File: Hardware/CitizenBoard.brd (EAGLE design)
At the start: 50 x 50 mm, 30 parts, among them IC1 MEGA8-P, J1 DCJ0202, J2 AUDIO-JACK-3.5, Y1 16MHz

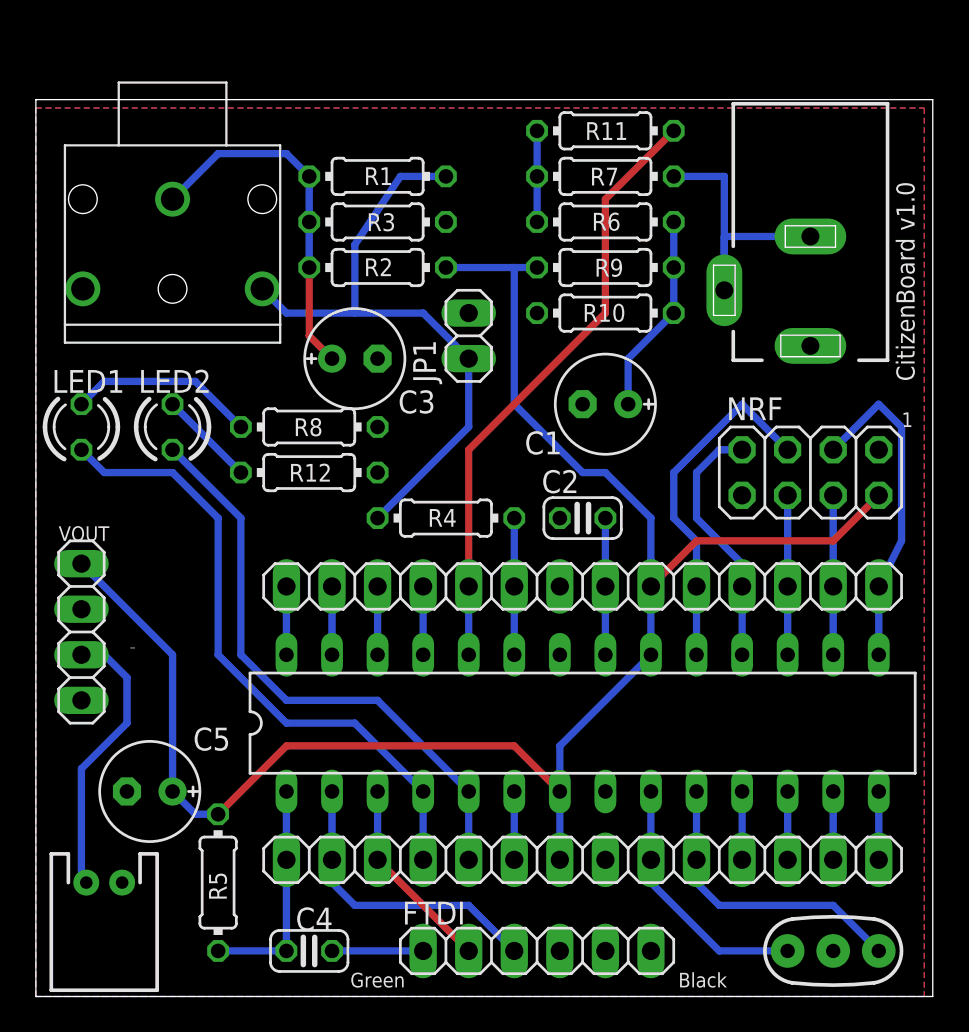
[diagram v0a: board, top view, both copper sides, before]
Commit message: Divers corrections de placement
Déplacement vers le haut de R1, R2, R3 et C3, pour les éloigner de R8.
Marquage de la polarisation des diodes et des condensateurs sur le silk.
Décalage du connecteur FTDI pour ne pas entrer en collision avec NRF
Décalage de C1 pour la même raison
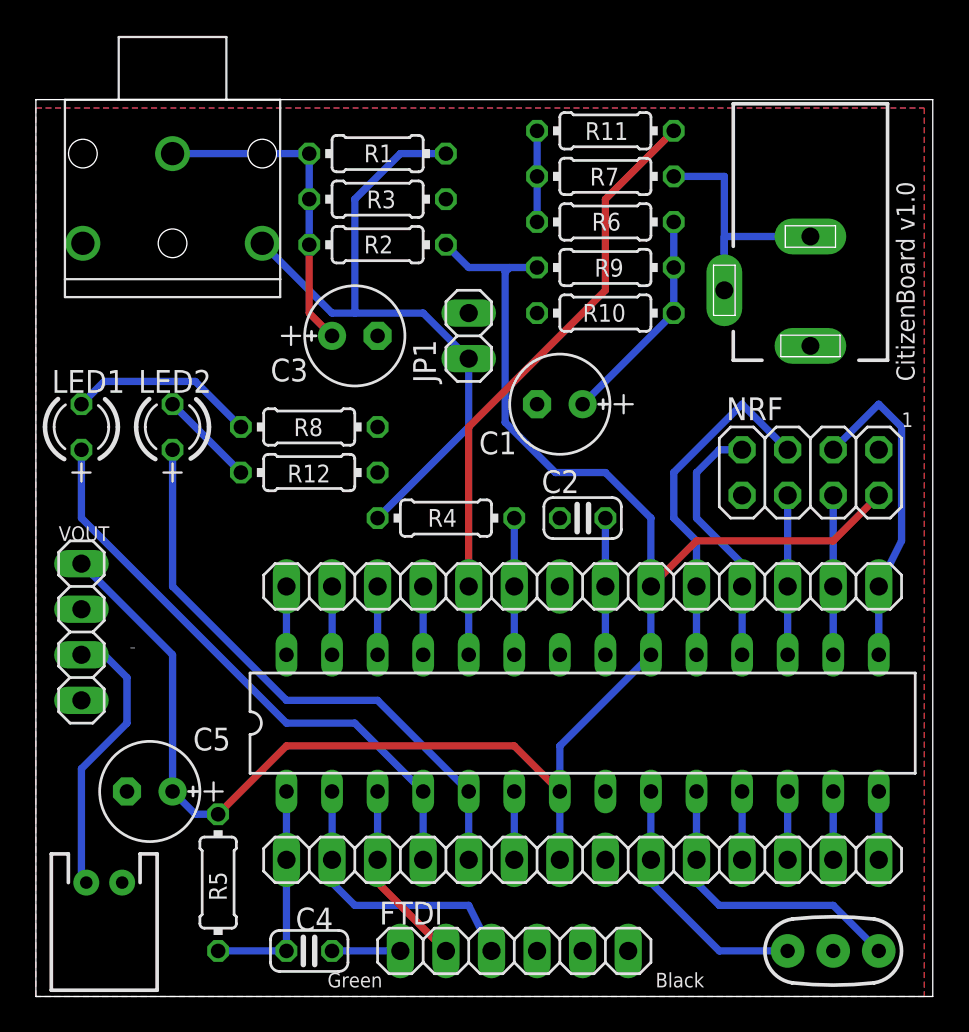
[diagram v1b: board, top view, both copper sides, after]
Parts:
- moved C1 2.54 mm to (29.2, 33.0)
- moved J2 2.54 mm to (7.62, 47.0)
- moved R1 1.27 mm to (19.1, 47.0)
- moved R3 1.27 mm to (19.1, 44.5)
- moved FTDI 1.27 mm to (26.7, 2.54)
- moved C3 1.27 mm to (17.8, 36.8)
- moved R2 1.27 mm to (19.1, 41.9)
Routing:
- net N: track 35.0 -> 37.6 mm
- net D2: track 35.2 -> 33.0 mm
- net VCC: track 98.5 -> 100.2 mm
- net N$4: track 19.9 -> 18.3 mm
- net N$3: track 5.08 -> 3.81 mm
- net N$11: track 11.2 -> 12.3 mm
- net RX: track 16.8 -> 16.1 mm
- net TX: track 11.0 -> 10.5 mm

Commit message: Correction de l'empreinte du jack
Et modification de tracés pour le champ de masse
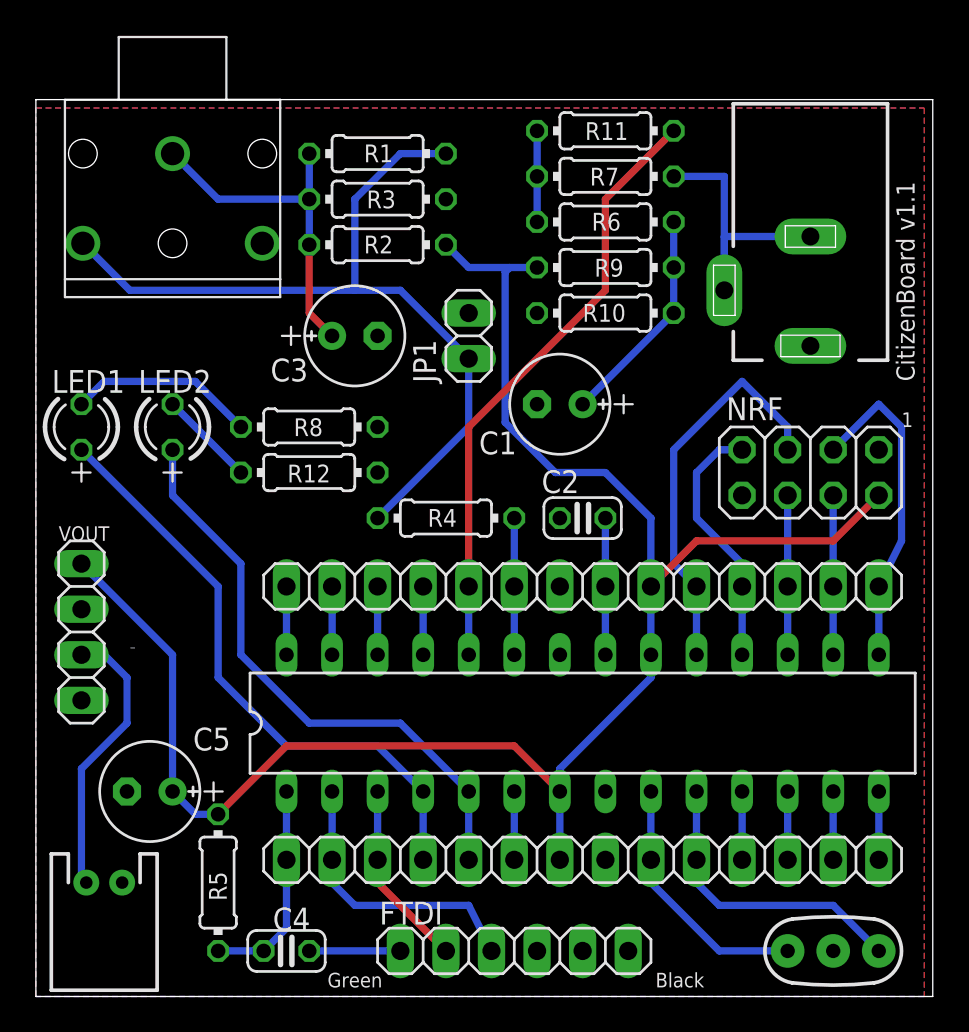
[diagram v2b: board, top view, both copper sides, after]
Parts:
- moved C4 1.27 mm to (14.0, 2.54)
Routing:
- net N: track 37.6 -> 46.4 mm
- net SCK: track 19.7 -> 22.2 mm
- net N$3: track 3.81 -> 5.08 mm
- net N$4: track 18.3 -> 19.4 mm
- net D2: track 33.0 -> 33.7 mm
- net RESET: track 12.7 -> 12.0 mm
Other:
- board text added: "CitizenBoard v1.1"
- board text removed: "CitizenBoard v1.0"
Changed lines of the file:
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@@
 <setting verticaltext="up"/>
 </settings>
-<grid distance="0.01" unitdist="inch" unit="inch" style="dots" multiple="1" display="yes" altdistance="0.025" altunitdist="inch" altunit="inch"/>
+<grid distance="0.05" unitdist="inch" unit="inch" style="dots" multiple="1" display="yes" altdistance="0.025" altunitdist="inch" altunit="inch"/>
 <layers>
-<layer number="1" name="Top" color="4" fill="1" visible="yes" active="yes"/>
+<layer number="1" name="Top" color="4" fill="1" visible="no" active="yes"/>
 <layer number="16" name="Bottom" color="1" fill="1" visible="yes" active="yes"/>
 <layer number="17" name="Pads" color="2" fill="1" visible="yes" active="yes"/>
@@
 <rectangle x1="4.84631875" y1="47.64608125" x2="5.94868125" y2="47.6885" layer="22"/>
 <text x="0" y="-0.21081875" size="0.08381875" layer="22" font="vector" rot="MR0">/home/phyks/hackEns/CitizenWatt/CitizenWatt-sensor/Hardware/silkscreen3bold.bmp</text>
-<text x="48.9894625" y="34.296859375" size="1.016" layer="21" font="vector" rot="R90">CitizenBoard v1.0</text>
+<text x="48.9894625" y="34.296859375" size="1.016" layer="21" font="vector" rot="R90">CitizenBoard v1.1</text>
 <wire x1="2.54" y1="29.718" x2="2.54" y2="28.702" width="0.127" layer="21"/>
 <wire x1="2.032" y1="29.21" x2="3.048" y2="29.21" width="0.127" layer="21"/>
@@
 <attribute name="VALUE" x="21.2344" y="26.1874" size="0.9906" layer="27" ratio="10"/>
 </element>
-<element name="C4" library="rcl" package="C025-024X044" value="0.1 µF 6V" x="15.24" y="2.54" smashed="yes" rot="R180">
-<attribute name="NAME" x="14.478" y="3.683" size="1.27" layer="25" ratio="10"/>
-<attribute name="VALUE" x="17.018" y="5.207" size="1.27" layer="27" ratio="10" rot="R180"/>
+<element name="C4" library="rcl" package="C025-024X044" value="0.1 µF 6V" x="13.97" y="2.54" smashed="yes" rot="R180">
+<attribute name="NAME" x="13.208" y="3.683" size="1.27" layer="25" ratio="10"/>
+<attribute name="VALUE" x="15.748" y="5.207" size="1.27" layer="27" ratio="10" rot="R180"/>
 </element>
 <element name="R5" library="rcl" package="0204/7" value="10K" x="10.16" y="6.35" smashed="yes" rot="R90">
@@
 <wire x1="29.21" y1="11.43" x2="29.21" y2="7.62" width="0.4064" layer="16"/>
 <wire x1="34.29" y1="22.86" x2="34.29" y2="19.05" width="0.4064" layer="16"/>
-<wire x1="29.21" y1="11.43" x2="29.21" y2="13.97" width="0.4064" layer="16"/>
-<wire x1="29.21" y1="13.97" x2="34.29" y2="19.05" width="0.4064" layer="16"/>
 <contactref element="C5" pad="+"/>
 <contactref element="JP5" pad="4"/>
@@
 <wire x1="26.162" y1="32.004" x2="26.162" y2="40.386" width="0.4064" layer="16"/>
 <wire x1="26.162" y1="40.386" x2="26.416" y2="40.64" width="0.4064" layer="16"/>
+<wire x1="29.21" y1="11.43" x2="29.21" y2="12.7" width="0.4064" layer="16"/>
+<wire x1="29.21" y1="12.7" x2="34.29" y2="17.78" width="0.4064" layer="16"/>
+<wire x1="34.29" y1="17.78" x2="34.29" y2="19.05" width="0.4064" layer="16"/>
 </signal>
 <signal name="RX">
@@
 <contactref element="IC1" pad="19"/>
 <wire x1="36.83" y1="19.05" x2="36.83" y2="22.86" width="0.4064" layer="16"/>
-<wire x1="36.83" y1="22.86" x2="36.83" y2="25.4" width="0.4064" layer="16"/>
-<wire x1="36.83" y1="25.4" x2="35.56" y2="26.67" width="0.4064" layer="16"/>
-<wire x1="35.56" y1="26.67" x2="35.56" y2="29.21" width="0.4064" layer="16"/>
-<wire x1="35.56" y1="29.21" x2="39.37" y2="33.02" width="0.4064" layer="16"/>
-<wire x1="39.37" y1="33.02" x2="41.91" y2="30.48" width="0.4064" layer="16"/>
+<wire x1="36.83" y1="22.86" x2="35.56" y2="24.13" width="0.4064" layer="16"/>
+<wire x1="35.56" y1="24.13" x2="35.56" y2="30.48" width="0.4064" layer="16"/>
+<wire x1="35.56" y1="30.48" x2="39.37" y2="34.29" width="0.4064" layer="16"/>
+<wire x1="41.91" y1="30.48" x2="41.91" y2="31.75" width="0.4064" layer="16"/>
+<wire x1="41.91" y1="31.75" x2="39.37" y2="34.29" width="0.4064" layer="16"/>
 </signal>
 <signal name="MISO">
@@
 <contactref element="IC1" pad="1"/>
 <wire x1="13.97" y1="7.62" x2="13.97" y2="11.43" width="0.4064" layer="16"/>
-<wire x1="13.97" y1="7.62" x2="13.97" y2="2.54" width="0.4064" layer="16"/>
-<wire x1="10.16" y1="2.54" x2="13.97" y2="2.54" width="0.4064" layer="16"/>
+<wire x1="10.16" y1="2.54" x2="12.7" y2="2.54" width="0.4064" layer="16"/>
+<wire x1="12.7" y1="2.54" x2="13.97" y2="3.81" width="0.4064" layer="16"/>
+<wire x1="13.97" y1="3.81" x2="13.97" y2="7.62" width="0.4064" layer="16"/>
 </signal>
 <signal name="TOSC1">
@@
 <wire x1="15.24" y1="44.45" x2="15.24" y2="41.91" width="0.4064" layer="16"/>
 <wire x1="15.24" y1="44.45" x2="15.24" y2="46.99" width="0.4064" layer="16"/>
-<wire x1="7.62" y1="46.99" x2="15.24" y2="46.99" width="0.4064" layer="16"/>
 <wire x1="15.24" y1="41.91" x2="15.24" y2="38.1" width="0.4064" layer="1"/>
 <wire x1="15.24" y1="38.1" x2="16.51" y2="36.83" width="0.4064" layer="1"/>
+<wire x1="7.62" y1="46.99" x2="10.16" y2="44.45" width="0.4064" layer="16"/>
+<wire x1="10.16" y1="44.45" x2="15.24" y2="44.45" width="0.4064" layer="16"/>
 </signal>
 <signal name="N">
@@
 <wire x1="22.86" y1="46.99" x2="20.32" y2="46.99" width="0.4064" layer="16"/>
 <wire x1="20.32" y1="46.99" x2="17.78" y2="44.45" width="0.4064" layer="16"/>
-<wire x1="17.78" y1="44.45" x2="17.78" y2="38.1" width="0.4064" layer="16"/>
-<wire x1="12.62" y1="41.99" x2="16.51" y2="38.1" width="0.4064" layer="16"/>
-<wire x1="16.51" y1="38.1" x2="17.78" y2="38.1" width="0.4064" layer="16"/>
-<wire x1="17.78" y1="38.1" x2="21.59" y2="38.1" width="0.4064" layer="16"/>
-<wire x1="21.59" y1="38.1" x2="24.13" y2="35.56" width="0.4064" layer="16"/>
+<wire x1="17.78" y1="44.45" x2="17.78" y2="39.37" width="0.4064" layer="16"/>
+<wire x1="17.78" y1="39.37" x2="20.32" y2="39.37" width="0.4064" layer="16"/>
+<wire x1="20.32" y1="39.37" x2="24.13" y2="35.56" width="0.4064" layer="16"/>
 <wire x1="19.05" y1="26.67" x2="24.13" y2="31.75" width="0.4064" layer="16"/>
 <wire x1="24.13" y1="31.75" x2="24.13" y2="35.56" width="0.4064" layer="16"/>
+<wire x1="17.78" y1="39.37" x2="5.24" y2="39.37" width="0.4064" layer="16"/>
+<wire x1="5.24" y1="39.37" x2="2.62" y2="41.99" width="0.4064" layer="16"/>
 </signal>
 <signal name="N$3">
 <contactref element="C4" pad="1"/>
 <contactref element="FTDI" pad="6"/>
-<wire x1="16.51" y1="2.54" x2="20.32" y2="2.54" width="0.4064" layer="16"/>
+<wire x1="15.24" y1="2.54" x2="20.32" y2="2.54" width="0.4064" layer="16"/>
 </signal>
 <signal name="D8">
@@
 <contactref element="IC1" pad="24"/>
 <wire x1="24.13" y1="19.05" x2="24.13" y2="22.86" width="0.4064" layer="16"/>
-<wire x1="31.75" y1="38.1" x2="31.75" y2="39.37" width="0" layer="19" extent="1-16"/>
 <wire x1="31.75" y1="44.45" x2="35.56" y2="48.26" width="0.4064" layer="1"/>
 <wire x1="24.13" y1="22.86" x2="24.13" y2="31.75" width="0.4064" layer="1"/>
@@
 <contactref element="JP2" pad="4"/>
 <wire x1="21.59" y1="7.62" x2="21.59" y2="11.43" width="0.4064" layer="16"/>
-<wire x1="21.59" y1="11.43" x2="17.78" y2="15.24" width="0.4064" layer="16"/>
-<wire x1="17.78" y1="15.24" x2="13.97" y2="15.24" width="0.4064" layer="16"/>
-<wire x1="13.97" y1="15.24" x2="2.54" y2="26.67" width="0.4064" layer="16"/>
-<wire x1="2.54" y1="26.67" x2="2.54" y2="30.48" width="0.4064" layer="16"/>
+<wire x1="21.59" y1="11.43" x2="19.05" y2="13.97" width="0.4064" layer="16"/>
+<wire x1="19.05" y1="13.97" x2="13.97" y2="13.97" width="0.4064" layer="16"/>
+<wire x1="13.97" y1="13.97" x2="10.16" y2="17.78" width="0.4064" layer="16"/>
+<wire x1="10.16" y1="17.78" x2="10.16" y2="22.86" width="0.4064" layer="16"/>
+<wire x1="10.16" y1="22.86" x2="2.54" y2="30.48" width="0.4064" layer="16"/>
 </signal>
 <signal name="D3">
@@
 <contactref element="JP2" pad="5"/>
 <wire x1="24.13" y1="11.43" x2="24.13" y2="7.62" width="0.4064" layer="16"/>
-<wire x1="13.97" y1="16.51" x2="19.05" y2="16.51" width="0.4064" layer="16"/>
-<wire x1="19.05" y1="16.51" x2="24.13" y2="11.43" width="0.4064" layer="16"/>
-<wire x1="13.97" y1="16.51" x2="7.62" y2="22.86" width="0.4064" layer="16"/>
-<wire x1="7.62" y1="22.86" x2="7.62" y2="30.48" width="0.4064" layer="16"/>
+<wire x1="24.13" y1="11.43" x2="20.32" y2="15.24" width="0.4064" layer="16"/>
+<wire x1="20.32" y1="15.24" x2="15.24" y2="15.24" width="0.4064" layer="16"/>
+<wire x1="15.24" y1="15.24" x2="11.43" y2="19.05" width="0.4064" layer="16"/>
+<wire x1="11.43" y1="19.05" x2="11.43" y2="24.13" width="0.4064" layer="16"/>
+<wire x1="11.43" y1="24.13" x2="7.62" y2="27.94" width="0.4064" layer="16"/>
+<wire x1="7.62" y1="27.94" x2="7.62" y2="30.48" width="0.4064" layer="16"/>
 </signal>
 <signal name="D4">

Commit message: Mesure de la valeur de la batterie
via un solder pad
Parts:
- added SJ1: (no value), jumper:SJ
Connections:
- net ADC2: now also SJ1.1
- net VIN: now also SJ1.2
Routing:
- net ADC2: track 3.81 -> 19.1 mm
- net VIN: track 15.7 -> 20.0 mm
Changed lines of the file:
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@@
 <grid distance="0.05" unitdist="inch" unit="inch" style="dots" multiple="1" display="yes" altdistance="0.025" altunitdist="inch" altunit="inch"/>
 <layers>
-<layer number="1" name="Top" color="4" fill="1" visible="no" active="yes"/>
+<layer number="1" name="Top" color="4" fill="1" visible="yes" active="yes"/>
 <layer number="16" name="Bottom" color="1" fill="1" visible="yes" active="yes"/>
 <layer number="17" name="Pads" color="2" fill="1" visible="yes" active="yes"/>
@@
 <attribute name="VALUE" x="5.715" y="15.24" size="1.27" layer="27" rot="R90"/>
 </element>
+<element name="SJ1" library="jumper" package="SJ" value="" x="7.62" y="19.05" smashed="yes" rot="R180">
+<attribute name="VALUE" x="7.2199" y="19.05" size="0.02" layer="27" rot="R180"/>
+</element>
 </elements>
 <signals>
@@
 <contactref element="JP3" pad="4"/>
 <wire x1="21.59" y1="22.86" x2="21.59" y2="19.05" width="0.4064" layer="16"/>
+<contactref element="SJ1" pad="1"/>
+<wire x1="8.382" y1="19.05" x2="10.922" y2="16.51" width="0.4064" layer="1"/>
+<wire x1="10.922" y1="16.51" x2="19.05" y2="16.51" width="0.4064" layer="1"/>
+<wire x1="19.05" y1="16.51" x2="21.59" y2="19.05" width="0.4064" layer="1"/>
 </signal>
 <signal name="ADC3">
@@
 <wire x1="5.08" y1="17.78" x2="3.81" y2="19.05" width="0.4064" layer="16"/>
 <wire x1="3.81" y1="19.05" x2="2.54" y2="19.05" width="0.4064" layer="16"/>
+<contactref element="SJ1" pad="2"/>
+<wire x1="6.858" y1="19.05" x2="2.54" y2="19.05" width="0.4064" layer="1"/>
 </signal>
 <signal name="SHND">
